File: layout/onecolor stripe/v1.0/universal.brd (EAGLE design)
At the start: 38 x 33 mm, 39 parts, among them IC2 FT232RL, Q1 PSMN2R0-30YL, Q2 PSMN2R0-30YL, Q3 PSMN2R0-30YL, Q4 PSMN2R0-30YL, T1 BC848, T2 BC848, X1 6PIN_MDF6-6DP-3.5DS, X4 1PIN_SCHRAUBKLEMME, X5 1PIN_SCHRAUBKLEMME, X6 1PIN_SCHRAUBKLEMME

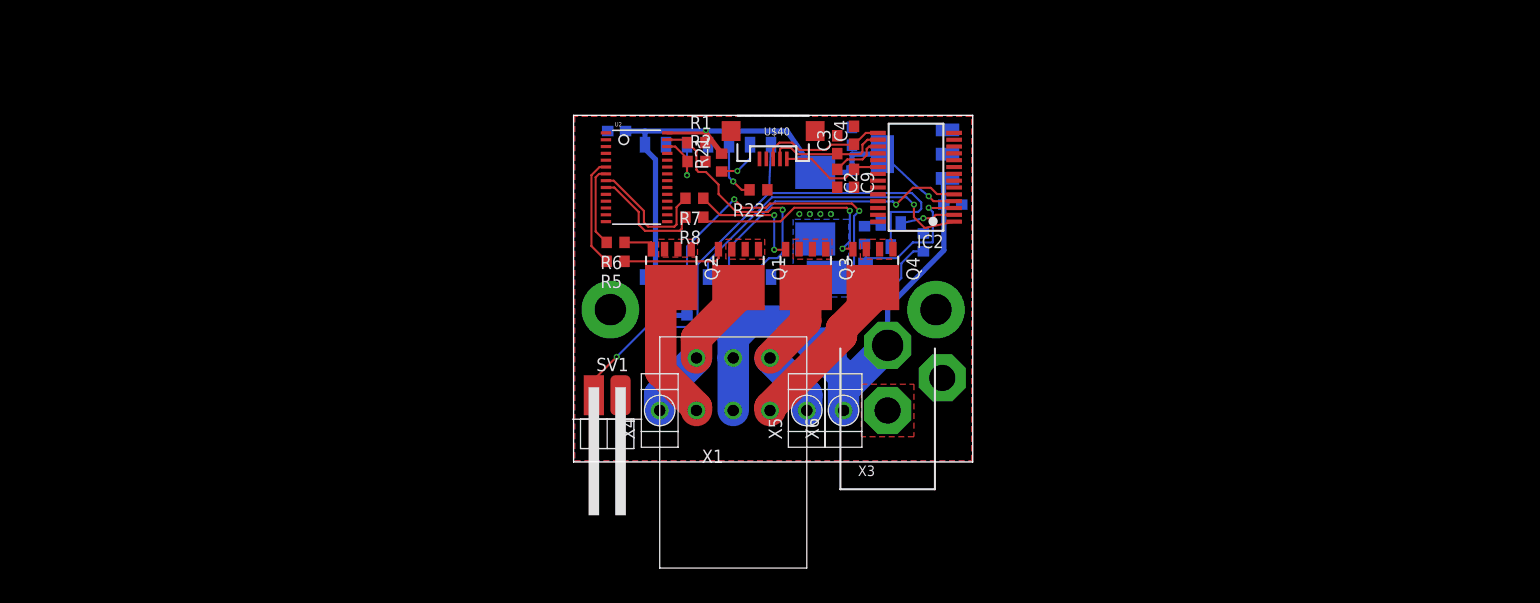
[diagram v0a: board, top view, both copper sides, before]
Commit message: Finished layout for 4*RGBW stripe v1.0
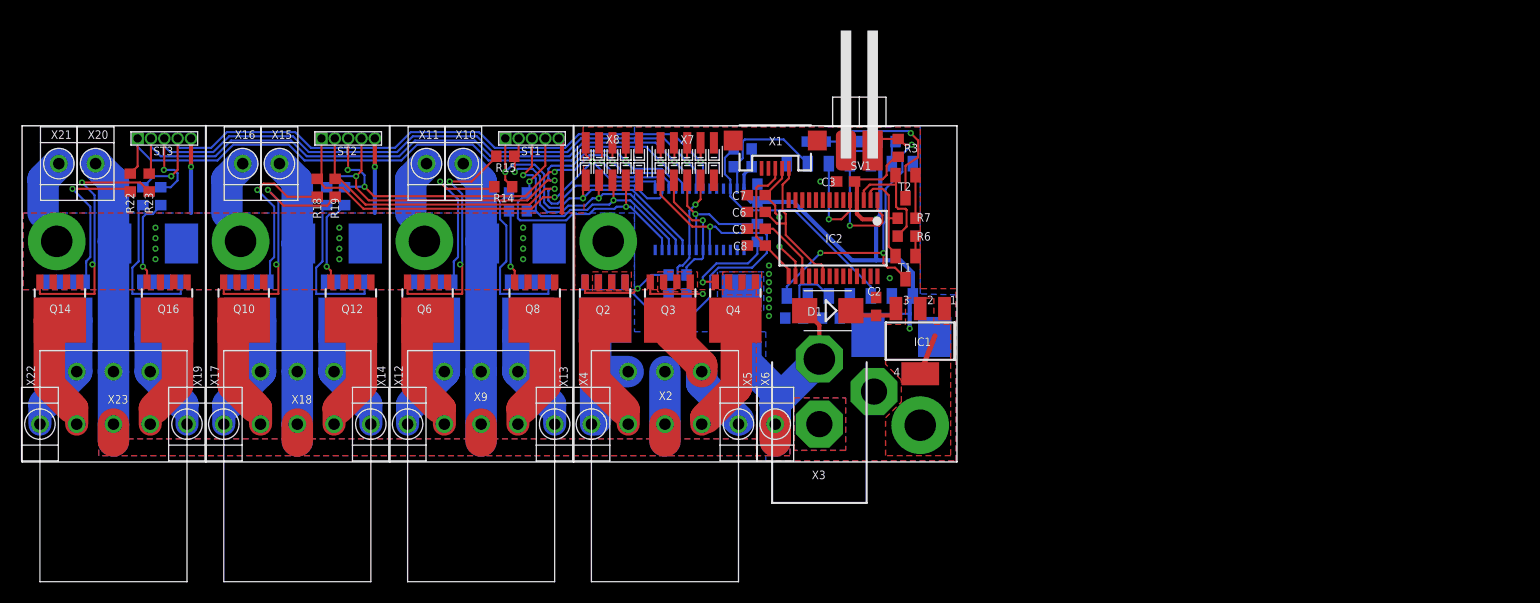
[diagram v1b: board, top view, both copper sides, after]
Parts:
- removed U$2: ESP8266, ESP8266:ESP-03
- removed U$40: USB-B, sid:USB-MICROB
- removed U2: (no value), adafruit:TSSOP28
- added C10: 100n, rcl:C0603
- added C11, C12, C13: 100u, cap-master:7343-TE-D
- added D1: MBRS240, diode:SMB
- added Q10, Q11, Q12, Q13, Q14, Q15, Q16, Q5, Q6, Q7, Q8, Q9: PSMN2R0-30YL, transistor-yaala:SOT669
- added R10, R11, R12, R13, R14, R15, R16, R17, R18, R24, R25, R9: 1k, rcl-2:R0603
- added ST1, ST2, ST3: 5PIN_STIFTLEISTE_1,27MM, con-yaala:5PIN_STIFTLEISTE_1,27MM
- added U$1: ESP8266, ESP8266:ESP-03
- added U1: (no value), adafruit:TSSOP28
- added X10, X11, X12, X13, X15, X16, X17, X18, X20, X21, X22, X23: 1PIN_SCHRAUBKLEMME, con-yaala:1PIN_SCHRAUBKLEMME
- added X14, X19, X2, X9: 6PIN_MDF6-6DP-3.5DS, con-yaala:MDF6-6DP-3.5DS
- added X7, X8: 10PIN_LEOTRONICS_1296-10, con-yaala:1296-10
- C3: value 22p -> 100n
- C4: value 22p -> 100u; device rcl:C0603 -> cap-master:7343-TE-D
- C6: value 100u -> 100n; device cap-master:7343-TE-D -> rcl:C0603
- C7, C8: value 100n -> 22p
- R1, R2, R5, R6, R7: value 1k -> 10k
- R19, R20, R21, R22, R23: value 10k -> 1k
- X1: value 6PIN_MDF6-6DP-3.5DS -> USB-B; device con-yaala:MDF6-6DP-3.5DS -> sid:USB-MICROB
- moved R23 66.9 mm to (-40.4, 26.6), flipped to the top, turned to 270 degrees
- moved R22 59.8 mm to (-42.2, 26.6), turned to 270 degrees
- moved R21 36.0 mm to (-21.8, 25.3), flipped to the bottom, turned to 270 degrees
- moved R20 35.9 mm to (-23.5, 25.3)
- moved SV1 33.8 mm to (27.2, 29.9), turned to 0 degrees
- moved R19 33.5 mm to (-22.7, 26.1), flipped to the top
- moved R6 27.7 mm to (31.7, 21.5), turned to 0 degrees
- moved X1 22.0 mm to (19.2, 30.6), turned to 180 degrees
- moved R7 20.3 mm to (31.7, 23.2), turned to 0 degrees
- moved C4 19.7 mm to (31.2, 11.9), flipped to the bottom, turned to 180 degrees
- moved R1 18.1 mm to (29.8, 30.5), flipped to the bottom
- moved R5 17.8 mm to (21.0, 13.7), flipped to the bottom
- moved IC1 17.8 mm to (33.0, 11.5), flipped to the top, turned to 180 degrees
- moved R2 14.9 mm to (26.5, 30.5), flipped to the bottom, turned to 180 degrees
- moved C7 14.6 mm to (17.4, 25.4), flipped to the top, turned to 180 degrees
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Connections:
- removed net B: Q3.4, R7.1
- removed net G: Q2.4, R6.1
- removed net R: Q1.4, R5.1
- removed net W: Q4.4, R8.1
- new net B1: R13.1, U1.8, X7.5
- new net B2: R17.1, ST1.3, U1.12, X8.5
- new net B3: R21.1, ST2.3, U1.17, X8.6
- new net B4: R25.1, ST3.3, U1.21, X7.6
- new net D+: C8.1, IC2.15, X1.D+
- new net D-: C7.1, IC2.16, X1.D-
- new net G1: R11.1, U1.7, X7.3
- new net G2: R15.1, ST1.2, U1.11, X8.3
- new net G3: R19.1, ST2.2, U1.16, X8.4
- new net G4: R23.1, ST3.2, U1.20, X7.4
- new net N$15: Q7.MB, X13.1, X9.5
- new net N$16: Q8.MB, X9.6
- new net N$17: Q6.4, R15.2
- new net N$18: Q7.4, R16.2
- new net N$22: Q8.4, R17.2
- new net N$23: Q5.4, R14.2
- new net N$25: Q9.MB, X14.1, X17.1
- new net N$26: Q10.MB, X14.2
- new net N$27: Q11.MB, X14.5, X18.1
- new net N$28: Q12.MB, X14.6
- new net N$29: Q10.4, R19.2
- new net N$30: Q11.4, R20.2
- new net N$31: Q12.4, R21.2
- new net N$32: Q9.4, R18.2
- new net N$34: Q13.MB, X19.1, X22.1
- new net N$35: Q14.MB, X19.2
- new net N$36: Q15.MB, X19.5, X23.1
- new net N$37: Q16.MB, X19.6
- new net N$38: Q14.4, R23.2
- new net N$39: Q15.4, R24.2
- new net N$40: Q16.4, R25.2
- new net N$41: Q13.4, R22.2
- new net N$43: C2.1, D1.C, IC1.3
- new net R1: R10.2, U1.6, X7.1
- new net R2: R14.1, ST1.1, U1.10, X8.1
- new net R3: R18.1, ST2.1, U1.15, X8.2
- new net R4: R22.1, ST3.1, U1.19, X7.2
- new net W1: R12.1, U1.9, X7.7
- new net W2: R16.1, ST1.4, U1.13, X8.7
- new net W3: R20.1, ST2.4, U1.18, X8.8
- new net W4: R24.1, ST3.4, U1.22, X7.8
- net +12V: now also C11.+, C12.+, C13.+, D1.A, X10.1, X14.3, X14.4, X15.1, X19.3, X19.4, X2.3, X2.4, X20.1, X9.3, X9.4; no longer C5.1, IC1.3, X1.3, X1.4
- net +3V3: now also C10.1, C3.1, C4.+, R3.2, R4.2, R8.2, R9.2, U$1.VCC, U1.28; no longer C6.+, C7.1, C8.1, R19.2, R20.2, R21.2, R23.2, U$2.VCC, U2.28
- net +5V: now also C6.1, X1.VBUS; no longer C9.1, U$40.VBUS
- net GND: now also C10.2, C11.-, C12.-, C13.-, C4.-, C6.2, Q10.1, Q10.2, Q10.3, Q11.1, Q11.2, Q11.3, Q12.1, Q12.2, Q12.3, Q13.1, Q13.2, Q13.3, Q14.1, Q14.2, Q14.3, Q15.1, Q15.2, Q15.3, Q16.1, Q16.2, Q16.3, Q5.1, Q5.2, Q5.3, Q6.1, Q6.2, Q6.3, Q7.1, Q7.2, Q7.3, Q8.1, Q8.2, Q8.3, Q9.1, Q9.2, Q9.3, R5.1, ST1.5, ST2.5, ST3.5, U$1.GND, U1.1, U1.14, U1.2, U1.23, U1.24, U1.25, U1.3, U1.4, U1.5, X1.GND, X1.MT1, X1.MT2, X11.1, X16.1, X21.1, X7.10, X7.9, X8.10, X8.9; no longer C4.2, C6.-, R22.1, U$2.GND, U$40.GND, U$40.MT1, U$40.MT2, U2.1, U2.14, U2.2, U2.23, U2.24, U2.25, U2.3, U2.4, U2.5
- net GPIO0: now also R3.1, T1.3, U$1.GPIO0; no longer R23.1, T2.3, U$2.GPIO0
- net GPIO15: now also R5.2, U$1.GPIO15; no longer R22.2, U$2.GPIO15
- net N$1: now also X2.1; no longer X1.1
- net N$10: now also R7.2, T2.1; no longer R4.2, T1.1
- net N$11: now also R1.1, U$1.CH_PD; no longer R19.1, U$2.CH_PD
- net N$12: now also C9.1; no longer C2.1
- net N$13: now also R4.1, U$1.GPIO2; no longer R21.1, U$2.GPIO2
- net N$14: now also Q1.4, R10.1; no longer R5.2, U2.6
- net N$19: now also Q2.4, R11.2; no longer R6.2, U2.7
- net N$2: now also X2.2; no longer X1.2
- net N$20: now also Q3.4, R12.2; no longer R7.2, U2.8
- net N$21: now also Q4.4, R13.2; no longer R8.2, U2.9
- net N$3: now also Q5.MB, X12.1, X9.1; no longer C4.1, IC2.15, U$40.D+
- net N$4: now also X2.6; no longer X1.6
- net N$5: now also X2.5; no longer X1.5
- net N$6: now also Q6.MB, X9.2; no longer C3.1, IC2.16, U$40.D-
- net N$7: now also R6.1, T2.2; no longer R3.1, T1.2
- net N$8: now also R7.1, T1.2; no longer R4.1, T2.2
- net N$9: now also R6.2, T1.1; no longer R3.2, T2.1
- net RST: now also C5.1, R2.1, T2.3, U$1.GPIO18; no longer R20.1, T1.3, U$2.GPIO18
- net RX: now also U$1.URXD; no longer U$2.URXD
- net SCL: now also R9.1, U$1.GPIO12, U1.26; no longer R2.1, U$2.GPIO12, U2.26
- net SDA: now also R8.1, U$1.NC, U1.27; no longer R1.1, U$2.NC, U2.27
- net TX: now also U$1.UTXD; no longer U$2.UTXD
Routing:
- net +12V: track 47.9 -> 119.2 mm
- net B4: track 0.00 -> 66.4 mm, vias 0 -> 2
- net W4: track 0.00 -> 66.1 mm, vias 0 -> 2
- net R4: track 0.00 -> 63.6 mm, vias 0 -> 1
- net G4: track 0.00 -> 63.1 mm, vias 0 -> 1
- net G3: track 0.00 -> 50.2 mm, vias 0 -> 2
- net W3: track 0.00 -> 46.3 mm, vias 0 -> 4
- net R3: track 0.00 -> 43.1 mm, vias 0 -> 2
- net B3: track 0.00 -> 42.4 mm, vias 0 -> 4
- net GND: track 0.00 -> 37.6 mm, vias 6 -> 27
- net R2: track 0.00 -> 30.8 mm, vias 0 -> 2
- net R1: track 0.00 -> 28.4 mm, vias 0 -> 1
- net W2: track 0.00 -> 28.1 mm, vias 0 -> 2
- net G2: track 0.00 -> 28.0 mm, vias 0 -> 2
- net B2: track 0.00 -> 27.2 mm, vias 0 -> 2
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- added copper zone on layer 1, net +12V
- added copper zone on layer 16, net +12V
- added copper zone on layer 1, net +3V3
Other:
- board size 38 x 33 mm -> 89 x 32 mm

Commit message: DRC errors and airwires in onecolor stripe removed.
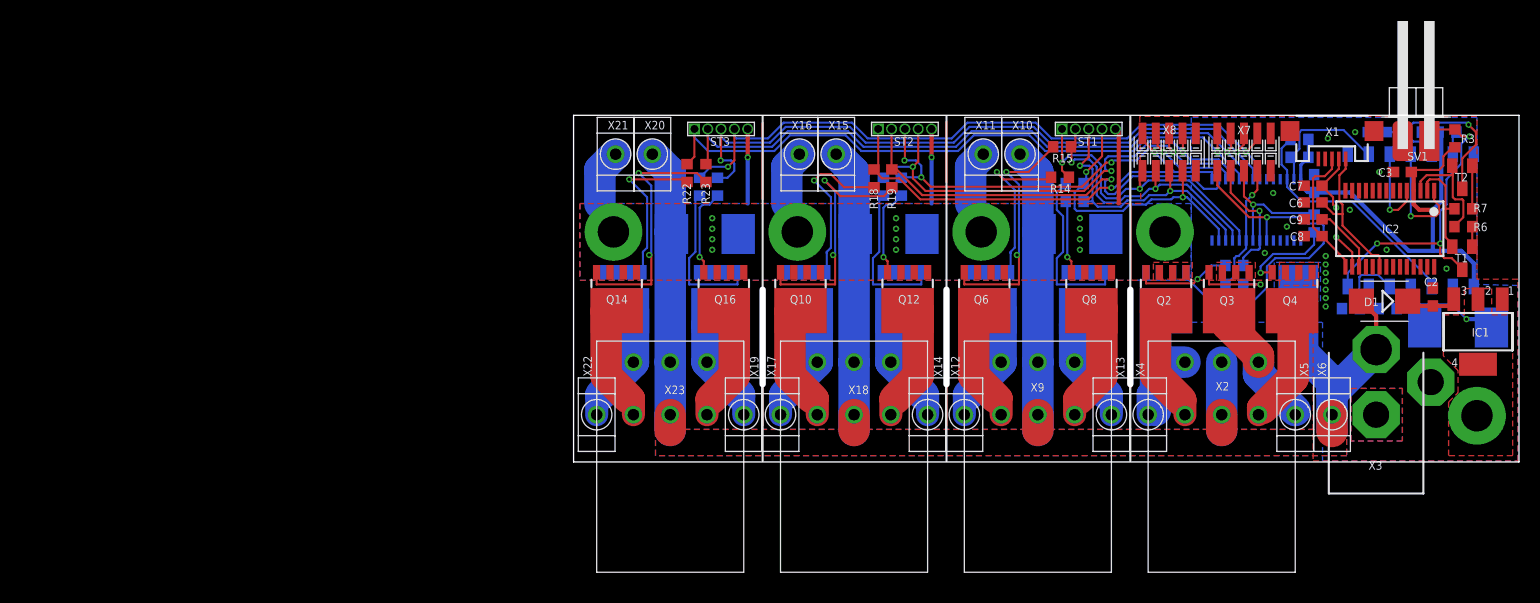
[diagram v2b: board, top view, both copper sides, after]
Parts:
- moved R1 53.4 mm to (83.2, 31.4)
- moved R2 53.4 mm to (79.9, 31.4)
- moved U$1 53.4 mm to (89.7, 16.9)
- moved C5 53.4 mm to (76.5, 31.4)
- moved Q1 53.4 mm to (56.4, 15.4)
- moved Q2 53.4 mm to (56.4, 15.4)
- moved Q3 53.2 mm to (62.4, 15.4)
- moved IC1 53.1 mm to (86.1, 12.4)
- moved C3 53.0 mm to (78.9, 27.6)
- moved C6 53.0 mm to (70.4, 24.7)
- moved C7 53.0 mm to (70.4, 26.3)
- moved C8 53.0 mm to (70.4, 21.5)
- moved C9 53.0 mm to (70.4, 23.1)
- moved Q4 53.0 mm to (68.4, 15.4)
- moved R3 53.0 mm to (83.9, 30.8)
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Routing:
- net N$46: track 0.00 -> 13.1 mm
- net N$201: track 0.00 -> 13.1 mm
- net N$48: track 0.00 -> 13.0 mm
- net N$47: track 0.00 -> 7.40 mm
- net N$44: track 0.00 -> 7.30 mm
- net N$45: track 0.00 -> 5.80 mm
- net N$1: track 13.9 -> 17.0 mm
- net +12V: track 119.2 -> 116.5 mm
- net R3: track 43.1 -> 44.4 mm
- net RST: track 20.0 -> 19.5 mm
- net GND: track 37.6 -> 37.3 mm, vias 27 -> 34
- net W3: vias 4 -> 3
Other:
- board size 89 x 32 mm -> 90 x 33 mm
